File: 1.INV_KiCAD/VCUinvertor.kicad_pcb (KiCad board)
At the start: 2 copper layers, 100.7 x 117.9 mm, 118 parts, among them J7 PowerSupply, J9 BRAKE LIGHT, K1 IM06, Q1 2N7002, Q10 2N7002, Q13 BC848C, Q2 2N7002, Q3 2N7002, Q4 2N7002, Q5 2N7002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

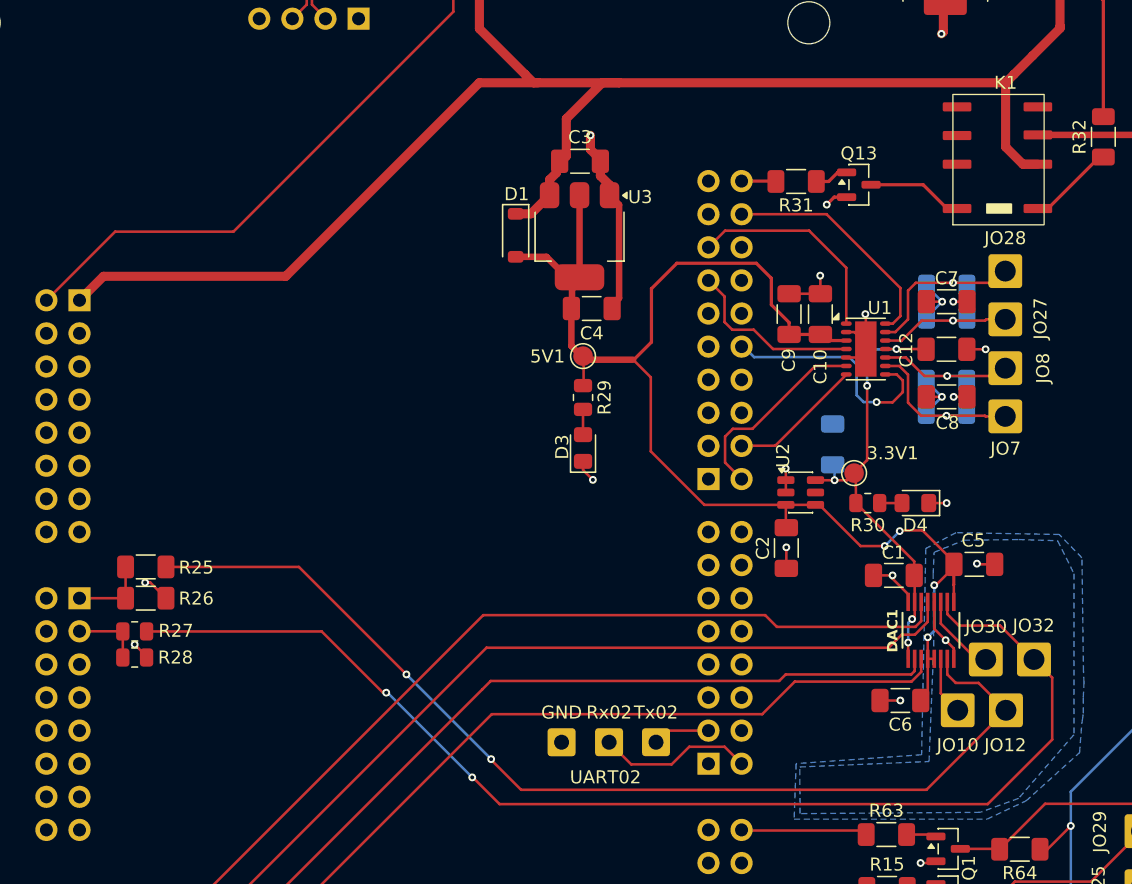
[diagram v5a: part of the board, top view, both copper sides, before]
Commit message: Relay NC to NO change
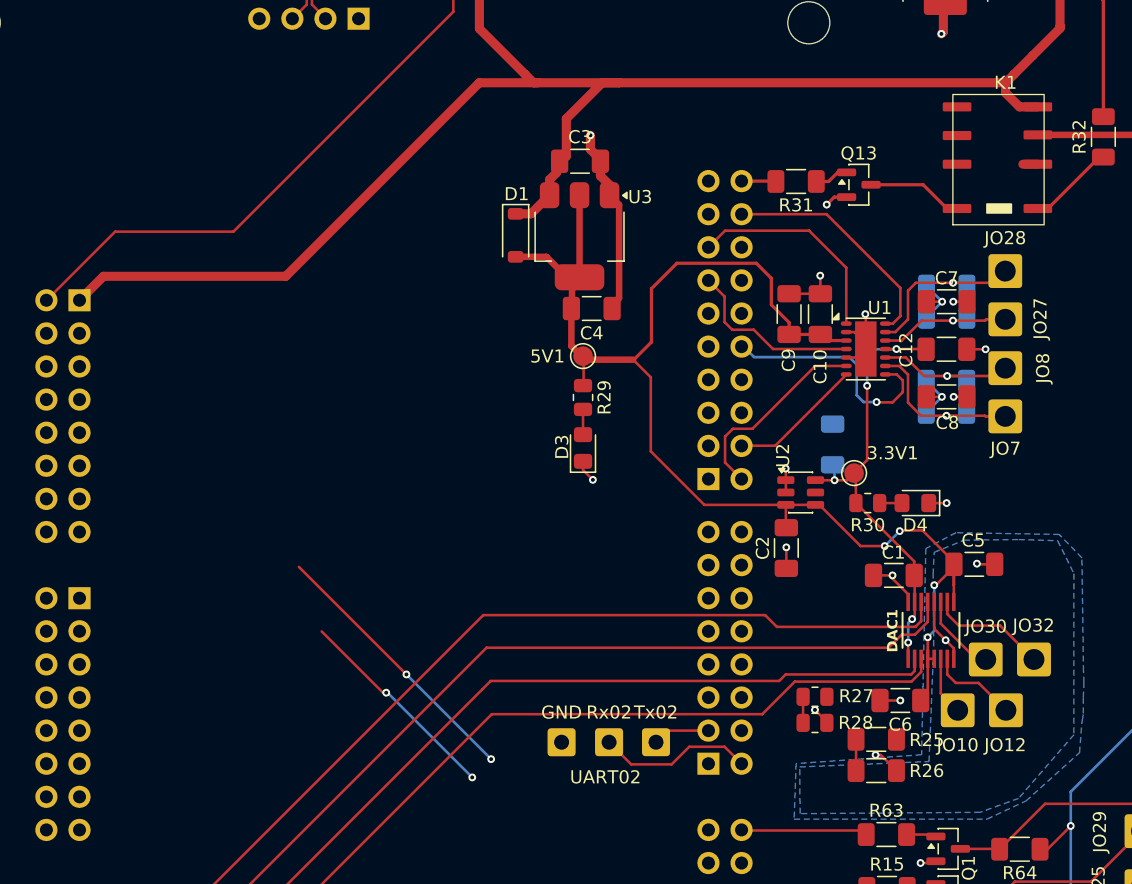
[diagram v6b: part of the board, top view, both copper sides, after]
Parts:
- K1: value IM06 -> IM06DGR
- moved R25 57.6 mm to (124.2, 116.7)
- moved R26 57.6 mm to (124.2, 119.1)
- moved R27 52.4 mm to (119.4, 113.5)
- moved R28 52.4 mm to (119.4, 115.5)
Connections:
- K1 pad 2: BAT+ -> unconnected-(K1-Pad2)
- K1 pad 4: unconnected-(K1-Pad4) -> BAT+
- NXP11 pad 1: unconnected-(NXP11-Pin_1-Pad1) -> NXP_TPSOUT01
- NXP11 pad 4: unconnected-(NXP11-Pin_4-Pad4) -> NXP_TPSOUT02
- NXP14 pad 1: NXP_TPSOUT01 -> unconnected-(NXP14-Pin_1-Pad1)
- NXP14 pad 3: NXP_TPSOUT02 -> unconnected-(NXP14-Pin_3-Pad3)
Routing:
- net /TPS2: track 92.8 -> 25.2 mm
- net /TPS1: track 80.9 -> 27.7 mm
- net BAT+: track 158.1 -> 153.9 mm
- net NXP_TPSOUT01: track 5.94 -> 2.40 mm
- net NXP_TPSOUT02: track 5.33 -> 2.18 mm
- net unconnected-(K1-Pad2): track 0.00 -> 1.15 mm
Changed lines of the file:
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@@
 	(footprint "Resistor_SMD:R_1206_3216Metric_Pad1.30x1.75mm_HandSolder"
 		(layer "F.Cu")
-		(at 68.10051 105.89274)
+		(at 124.15051 119.12274)
 		(descr "Resistor SMD 1206 (3216 Metric), square (rectangular) end terminal, IPC-7351 nominal with elongated pad for handsoldering. (Body size source: IPC-SM-782 page 72, https://www.pcb-3d.com/wordpress/wp-content/uploads/ipc-sm-782a_amendment_1_and_2.pdf), generated with kicad-footprint-generator")
 		(tags "resistor handsolder")
@@
 	(footprint "Resistor_SMD:R_0805_2012Metric"
 		(layer "F.Cu")
-		(at 67.25051 110.44274)
+		(at 119.44801 115.46024)
 		(descr "Resistor SMD 0805 (2012 Metric), square (rectangular) end terminal, IPC-7351 nominal, (Body size source: IPC-SM-782 page 72, https://www.pcb-3d.com/wordpress/wp-content/uploads/ipc-sm-782a_amendment_1_and_2.pdf), generated with kicad-footprint-generator")
 		(tags "resistor")
@@
 	(footprint "Resistor_SMD:R_0805_2012Metric"
 		(layer "F.Cu")
-		(at 67.25051 108.44274 180)
+		(at 119.44801 113.46024 180)
 		(descr "Resistor SMD 0805 (2012 Metric), square (rectangular) end terminal, IPC-7351 nominal, (Body size source: IPC-SM-782 page 72, https://www.pcb-3d.com/wordpress/wp-content/uploads/ipc-sm-782a_amendment_1_and_2.pdf), generated with kicad-footprint-generator")
 		(tags "resistor")
@@
 	(footprint "Resistor_SMD:R_1206_3216Metric_Pad1.30x1.75mm_HandSolder"
 		(layer "F.Cu")
-		(at 68.10051 103.49274 180)
+		(at 124.15051 116.72274 180)
 		(descr "Resistor SMD 1206 (3216 Metric), square (rectangular) end terminal, IPC-7351 nominal with elongated pad for handsoldering. (Body size source: IPC-SM-782 page 72, https://www.pcb-3d.com/wordpress/wp-content/uploads/ipc-sm-782a_amendment_1_and_2.pdf), generated with kicad-footprint-generator")
 		(tags "resistor handsolder")
@@
 			)
 		)
-		(property "Value" "IM06"
+		(property "Value" "IM06DGR"
 			(at 0 1 90)
 			(unlocked yes)
@@
 			(layers "F.Cu" "F.Mask" "F.Paste")
 			(roundrect_rratio 0.15)
-			(net "BAT+")
-			(pintype "passive")
+			(net "unconnected-(K1-Pad2)")
+			(pintype "passive+no_connect")
 		)
 		(pad "3" smd roundrect
@@
 			(layers "F.Cu" "F.Mask" "F.Paste")
 			(roundrect_rratio 0.15)
-			(net "unconnected-(K1-Pad4)")
-			(pintype "passive+no_connect")
+			(net "BAT+")
+			(pintype "passive")
 		)
 		(pad "5" smd roundrect
@@
 			(layers "*.Cu" "*.Mask")
 			(remove_unused_layers no)
-			(net "NXP_TPSOUT01")
+			(net "unconnected-(NXP14-Pin_1-Pad1)")
 			(pinfunction "Pin_1_1")
-			(pintype "passive")
+			(pintype "passive+no_connect")
 		)
 		(pad "2" thru_hole circle
@@
 			(layers "*.Cu" "*.Mask")
 			(remove_unused_layers no)
-			(net "NXP_TPSOUT02")
+			(net "unconnected-(NXP14-Pin_3-Pad3)")
 			(pinfunction "Pin_3_3")
-			(pintype "passive")
+			(pintype "passive+no_connect")
 		)
 		(pad "4" thru_hole circle
@@
 			(layers "*.Cu" "*.Mask")
 			(remove_unused_layers no)
-			(net "unconnected-(NXP11-Pin_1-Pad1)")
+			(net "NXP_TPSOUT01")
 			(pinfunction "Pin_1_1")
-			(pintype "passive+no_connect")
+			(pintype "passive")
 		)
 		(pad "2" thru_hole circle
@@
 			(layers "*.Cu" "*.Mask")
 			(remove_unused_layers no)
-			(net "unconnected-(NXP11-Pin_4-Pad4)")
+			(net "NXP_TPSOUT02")
 			(pinfunction "Pin_4_4")
-			(pintype "passive+no_connect")
+			(pintype "passive")
 		)
 		(pad "5" thru_hole circle
@@
 	)
 	(segment
-		(start 68.16301 110.44274)
-		(end 68.16301 110.35524)
+		(start 120.36051 115.46024)
+		(end 120.36051 115.37274)
 		(width 0.2)
 		(layer "F.Cu")
@@
 	)
 	(segment
-		(start 68.45051 104.69274)
-		(end 68.05051 104.69274)
+		(start 124.50051 117.92274)
+		(end 124.10051 117.92274)
 		(width 0.2)
 		(layer "F.Cu")
@@
 	)
 	(segment
-		(start 68.16301 110.35524)
-		(end 67.25051 109.44274)
+		(start 120.36051 115.37274)
+		(end 119.44801 114.46024)
 		(width 0.2)
 		(layer "F.Cu")
@@
 	)
 	(segment
-		(start 69.65051 105.89274)
-		(end 68.45051 104.69274)
+		(start 125.70051 119.12274)
+		(end 124.50051 117.92274)
 		(width 0.2)
 		(layer "F.Cu")
@@
 	)
 	(via
-		(at 68.05051 104.69274)
+		(at 124.10051 117.92274)
 		(size 0.6)
 		(drill 0.3)
@@
 	)
 	(via
-		(at 67.25051 109.44274)
+		(at 119.44801 114.46024)
 		(size 0.6)
 		(drill 0.3)
@@
 	)
 	(segment
-		(start 135.40051 72.59274)
-		(end 136.55051 72.59274)
-		(width 0.7)
-		(layer "F.Cu")
-		(net "BAT+")
-	)
-	(segment
 		(start 138.50051 56.94274)
 		(end 138.25051 56.94274)
@@
 	)
 	(segment
-		(start 134.07551 66.34274)
-		(end 134.07551 71.26774)
-		(width 0.7)
-		(layer "F.Cu")
-		(net "BAT+")
-	)
-	(segment
 		(start 97.654259 76.39899)
 		(end 99.08426 74.968989)
@@
 	)
 	(segment
+		(start 135.14051 68.19274)
+		(end 136.55051 68.19274)
+		(width 0.7)
+		(layer "F.Cu")
+		(net "BAT+")
+	)
+	(segment
 		(start 96.48176 76.39899)
 		(end 97.654259 76.39899)
@@
 	)
 	(segment
-		(start 93.70051 62.195491)
-		(end 97.20051 65.695491)
+		(start 134.07551 67.12774)
+		(end 135.14051 68.19274)
 		(width 0.7)
 		(layer "F.Cu")
@@
 	)
 	(segment
-		(start 134.07551 71.26774)
-		(end 135.40051 72.59274)
+		(start 93.70051 62.195491)
+		(end 97.20051 65.695491)
 		(width 0.7)
 		(layer "F.Cu")
@@
 	)
 	(segment
+		(start 134.07551 66.34274)
+		(end 134.07551 67.12774)
+		(width 0.7)
+		(layer "F.Cu")
+		(net "BAT+")
+	)
+	(segment
 		(start 134.722759 65.695491)
 		(end 134.07551 66.34274)
@@
 	)
 	(segment
-		(start 66.55051 105.89274)
-		(end 66.55051 103.49274)
-		(width 0.2)
-		(layer "F.Cu")
-		(net "NXP_TPSOUT01")
-	)
-	(segment
-		(start 66.55051 105.89274)
-		(end 63.01551 105.892741)
+		(start 122.60051 119.12274)
+		(end 122.60051 116.72274)
 		(width 0.2)
 		(layer "F.Cu")
@@
 	)
 	(segment
-		(start 66.33801 110.44274)
-		(end 66.33801 108.44274)
+		(start 118.53551 115.46024)
+		(end 118.53551 113.46024)
 		(width 0.2)
 		(layer "F.Cu")
@@
 	)
 	(segment
-		(start 63.01551 108.432741)
-		(end 66.328011 108.432741)
+		(start 113.93051 116.16774)
+		(end 113.81551 116.05274)
 		(width 0.2)
 		(layer "F.Cu")
@@
 	)
 	(segment
-		(start 66.328011 108.432741)
-		(end 66.33801 108.44274)
+		(start 118.525511 113.450241)
+		(end 118.53551 113.46024)
 		(width 0.2)
 		(layer "F.Cu")
@@
 	)
 	(segment
-		(start 95.25051 121.69274)
-		(end 93.20051 119.64274)
-		(width 0.2)
-		(layer "F.Cu")
-		(net "/TPS2")
-	)
-	(segment
-		(start 81.60051 108.44274)
-		(end 68.16301 108.44274)
-		(width 0.2)
-		(layer "F.Cu")
-		(net "/TPS2")
-	)
-	(segment
 		(start 130.48111 107.99274)
 		(end 133.65051 107.99274)
@@
 	)
 	(segment
-		(start 137.65051 111.99274)
-		(end 137.65051 116.74274)
-		(width 0.2)
-		(layer "F.Cu")
-		(net "/TPS2")
-	)
-	(segment
-		(start 136.25051 110.59274)
-		(end 137.65051 111.99274)
-		(width 0.2)
-		(layer "F.Cu")
-		(net "/TPS2")
-	)
-	(segment
-		(start 132.70051 121.69274)
-		(end 95.25051 121.69274)
-		(width 0.2)
-		(layer "F.Cu")
-		(net "/TPS2")
-	)
-	(segment
-		(start 137.65051 116.74274)
-		(end 132.70051 121.69274)
-		(width 0.2)
-		(layer "F.Cu")
-		(net "/TPS2")
-	)
-	(segment
 		(start 129.60013 106.17394)
 		(end 129.60013 107.11176)
@@
 		(net "/TPS2")
 	)
-	(segment
-		(start 93.20051 119.64274)
-		(end 93.15051 119.64274)
-		(width 0.2)
-		(layer "F.Cu")
-		(net "/TPS2")
-	)
 	(via
 		(at 93.15051 119.64274)
@@
 	)
 	(segment
-		(start 96.90051 120.59274)
-		(end 94.60051 118.29274)
-		(width 0.2)
-		(layer "F.Cu")
-		(net "/TPS1")
-	)
-	(segment
 		(start 129.60013 111.74236)
 		(end 130.25051 112.39274)
@@
 	)
 	(segment
-		(start 128.00051 120.59274)
-		(end 96.90051 120.59274)
-		(width 0.2)
-		(layer "F.Cu")
-		(net "/TPS1")
-	)
-	(segment
-		(start 79.85051 103.49274)
-		(end 69.65051 103.49274)
-		(width 0.2)
-		(layer "F.Cu")
-		(net "/TPS1")
-	)
-	(segment
-		(start 134.10051 114.49274)
-		(end 128.00051 120.59274)
-		(width 0.2)
-		(layer "F.Cu")
-		(net "/TPS1")
-	)
-	(segment
 		(start 132.00051 112.39274)
 		(end 134.10051 114.49274)
@@
 		(net "/TPS1")
 	)
-	(segment
-		(start 94.60051 118.29274)
-		(end 94.60051 118.24274)
-		(width 0.2)
-		(layer "F.Cu")
-		(net "/TPS1")
-	)
 	(via
 		(at 94.60051 118.24274)
@@
 	)
 	(segment
-		(start 113.93051 116.16774)
-		(end 113.81551 116.05274)
-		(width 0.2)
-		(layer "F.Cu")
-		(net "unconnected-(NXP11-Pin_4-Pad4)")
-	)
-	(segment
 		(start 113.81551 84.509471)
 		(end 113.81551 84.048741)
@@
 		(net "unconnected-(NXP10-Pin_14-Pad14)")
 	)
+	(segment
+		(start 135.40051 72.59274)
+		(end 136.55051 72.59274)
+		(width 0.7)
+		(layer "F.Cu")
+		(net "unconnected-(K1-Pad2)")
+	)
 	(zone

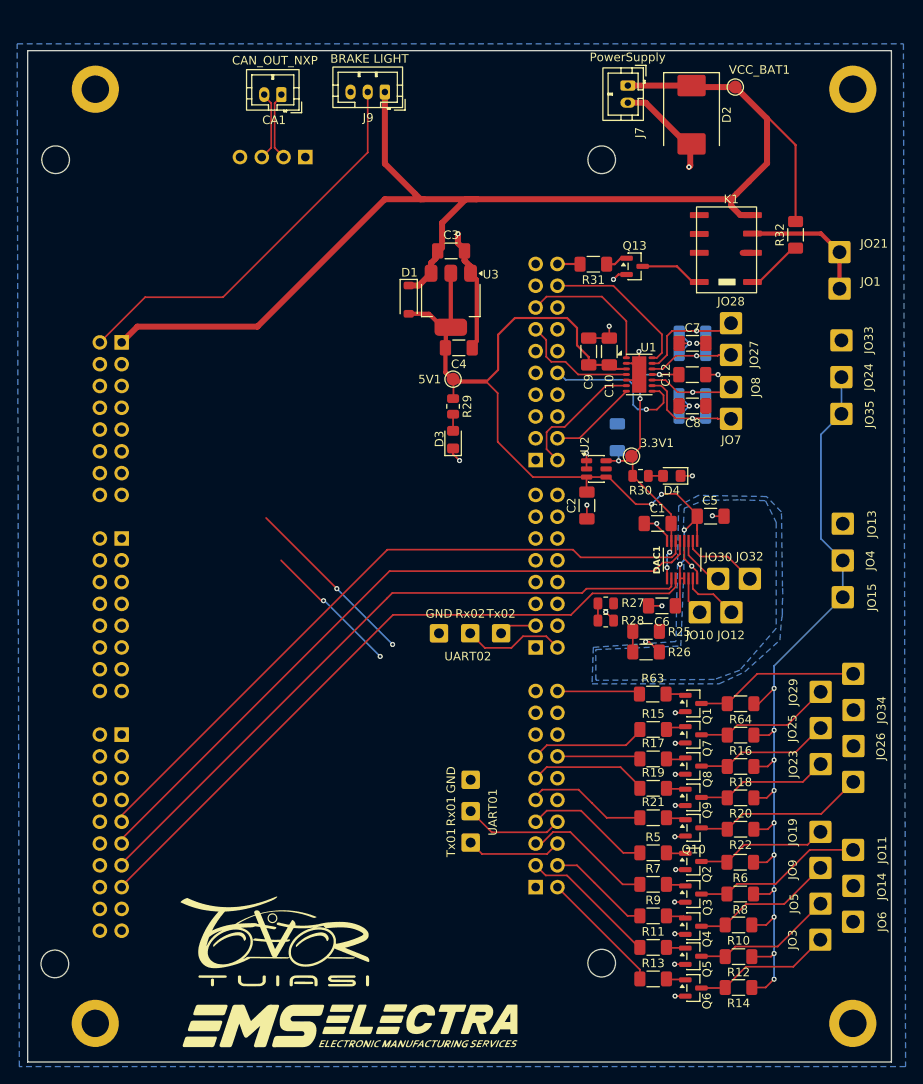
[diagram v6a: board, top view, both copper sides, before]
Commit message: Changes on NXPTPSOUT1&2
1. Switch The switch to NO from NC --> From pin 2 to pin 4
2.Move the connectors of the TPS OUT1 & 2
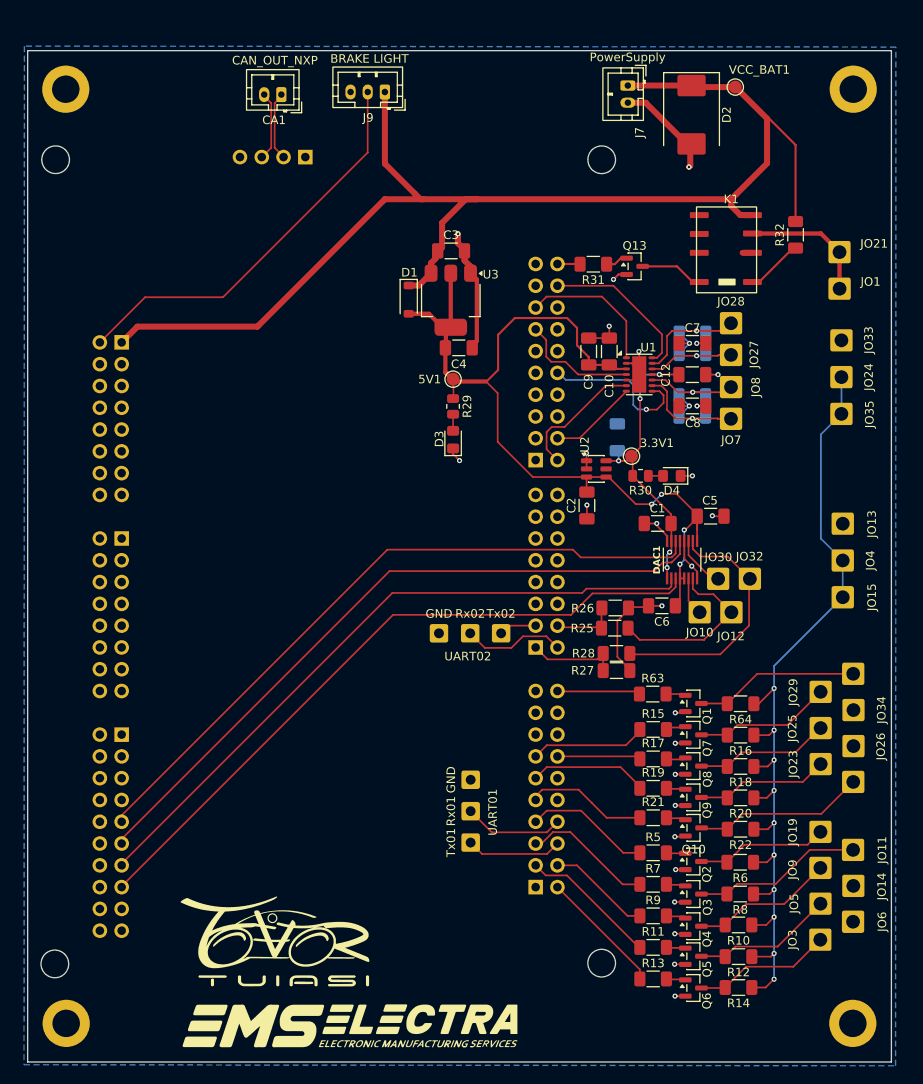
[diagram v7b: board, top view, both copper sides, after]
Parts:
- R27, R28: footprint Resistor_SMD:R_0805_2012Metric -> Resistor_SMD:R_1206_3216Metric_Pad1.30x1.75mm_HandSolder
- moved R26 6.27 mm to (120.6, 114.0)
- moved R27 5.97 mm to (120.7, 119.3)
- moved R28 5.97 mm to (120.7, 121.3)
- moved R25 3.67 mm to (120.5, 116.3)
- moved H2 3.45 mm to (56.5, 53.5)
- moved H3 3.39 mm to (56.6, 162.4)
- moved H1 0.05 mm to (148.3, 53.5)
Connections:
- NXP11 pad 1: NXP_TPSOUT01 -> NXP_TPSOUT02
- NXP11 pad 4: NXP_TPSOUT02 -> NXP_TPSOUT01
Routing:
- net NXP_TPSOUT02: track 2.18 -> 10.7 mm
- net GND: track 78.6 -> 86.0 mm, vias 28 -> 26
- net /TPS1: track 27.7 -> 20.8 mm, vias 2 -> 0
- net NXP_TPSOUT01: track 2.40 -> 7.63 mm
- net /TPS2: track 25.2 -> 29.9 mm, vias 2 -> 0
